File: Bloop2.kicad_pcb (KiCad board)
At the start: 2 copper layers, 15 parts, among them J1 Input, J2 Output, U1 TL072

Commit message: Feature complete device with first layout.
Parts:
- added C5: 1u, Capacitor_THT:CP_Radial_D5.0mm_P2.00mm, F.Cu at (171.4, 118.1)
- added C6: 1u, Capacitor_THT:CP_Radial_D5.0mm_P2.00mm, F.Cu at (135.9, 118.1)
- added D2: D, Diode_THT:D_DO-41_SOD81_P7.62mm_Horizontal, F.Cu at (153.7, 80.0)
- added J3: Input, Connector_Wire:SolderWirePad_1x02_P3.81mm_Drill1mm, F.Cu at (170.2, 82.5)
- added J4: Return, Connector_Wire:SolderWirePad_1x02_P3.81mm_Drill1mm, F.Cu at (137.2, 82.5)
- added J5: Send, Connector_Wire:SolderWirePad_1x02_P3.81mm_Drill1mm, F.Cu at (170.2, 129.5)
- added J6: Output, Connector_Wire:SolderWirePad_1x02_P3.81mm_Drill1mm, F.Cu at (137.2, 129.5)
- added R7: 10k, Resistor_THT:R_Axial_DIN0204_L3.6mm_D1.6mm_P7.62mm_Horizontal, F.Cu at (132.1, 105.4)
- added R8: 47k, Resistor_THT:R_Axial_DIN0204_L3.6mm_D1.6mm_P7.62mm_Horizontal, F.Cu at (175.3, 110.5)
- added R9: 47k, Resistor_THT:R_Axial_DIN0204_L3.6mm_D1.6mm_P7.62mm_Horizontal, F.Cu at (132.1, 110.5)
- added RV2: 10k, Connector_Wire:SolderWirePad_1x03_P3.175mm_Drill1mm, F.Cu at (133.3, 124.5)
- added SW1: 3PDT-A, Connector_Wire:SolderWirePad_1x03_P3.175mm_Drill1mm, F.Cu at (161.3, 120.7)
- added SW2: 3PDT-B, Connector_Wire:SolderWirePad_1x03_P3.175mm_Drill1mm, F.Cu at (174.0, 87.6)
- added SW3: 3PDT-C, Connector_Wire:SolderWirePad_1x03_P3.175mm_Drill1mm, F.Cu at (146.1, 114.3)
- C1: value 1u -> 47u; footprint Capacitor_THT:CP_Radial_D4.0mm_P2.00mm -> Capacitor_THT:CP_Radial_D6.3mm_P2.50mm
- C2: value 100u -> 47u; footprint Capacitor_THT:CP_Radial_D5.0mm_P2.00mm -> Capacitor_THT:CP_Radial_D6.3mm_P2.50mm
- C3: value 47u -> 1u; footprint Capacitor_THT:CP_Radial_D4.0mm_P2.00mm -> Capacitor_THT:CP_Radial_D5.0mm_P2.00mm
- C4: footprint Capacitor_THT:CP_Radial_D4.0mm_P2.00mm -> Capacitor_THT:CP_Radial_D5.0mm_P2.00mm
- D1: value D -> LED; footprint Diode_THT:D_DO-34_SOD68_P7.62mm_Horizontal -> LED_THT:LED_D5.0mm
- J1: value Input -> Power In; footprint Connector_Audio:Jack_3.5mm_CUI_SJ1-3533NG_Horizontal_CircularHoles -> Connector_BarrelJack:BarrelJack_CUI_PJ-102AH_Horizontal
- J2: value Output -> Power Out; footprint Connector_Audio:Jack_3.5mm_CUI_SJ1-3533NG_Horizontal_CircularHoles -> Connector_BarrelJack:BarrelJack_CUI_PJ-102AH_Horizontal
- R1: value 100k -> 2k7
- R4, R5: value 10k -> 100k
- R6: value 22k -> 10k
- RV1: footprint Connector_Wire:SolderWirePad_1x03_P3.175mm_Drill0.8mm -> Connector_Wire:SolderWirePad_1x03_P3.175mm_Drill1mm
- moved J1 67.6 mm to (165.1, 76.2), turned to 180 degrees
- moved C3 59.8 mm to (171.4, 100.3), turned to 90 degrees
- moved C2 49.4 mm to (160.0, 86.4), turned to 90 degrees
- moved J2 44.4 mm to (142.2, 76.2), turned to 180 degrees
- moved R6 41.4 mm to (175.3, 105.4), turned to 180 degrees
- moved R4 40.6 mm to (175.3, 92.7), turned to 180 degrees
- moved D1 34.9 mm to (153.7, 118.1), turned to 90 degrees
- moved C1 30.2 mm to (147.3, 86.4), turned to 90 degrees
- moved RV1 29.5 mm to (174.0, 124.5), turned to 180 degrees
- moved R1 29.0 mm to (149.9, 123.2)
- moved R3 26.2 mm to (156.2, 92.7), turned to 0 degrees
- moved R2 25.3 mm to (143.5, 92.7), turned to 0 degrees
- moved U1 14.4 mm to (157.5, 106.7), turned to 180 degrees
- moved C4 14.2 mm to (135.9, 100.3)
- moved R5 7.62 mm to (132.1, 92.7)
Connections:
- C1 pad 1: Net-(C1-Pad1) -> +9V
- C1 pad 2: Net-(C1-Pad2) -> GND
- C2 pad 1: +9V -> VREF
- C3 pad 2: GND -> Net-(C3-Pad2)
- D1 pad 1: +9V -> Net-(D1-Pad1)
- D1 pad 2: GND -> +9V
- R1 pad 1: Net-(C1-Pad2) -> Net-(D1-Pad1)
- R1 pad 2: GND -> Net-(R1-Pad2)
- R2 pad 2: Net-(C3-Pad1) -> VREF
- R3 pad 1: Net-(C3-Pad1) -> VREF
- R4 pad 1: Net-(C1-Pad1) -> Net-(C3-Pad2)
- R4 pad 2: Net-(C3-Pad1) -> GND
- R5 pad 1: Net-(C3-Pad1) -> Net-(C4-Pad2)
- R5 pad 2: Net-(R5-Pad2) -> GND
- R6 pad 1: Net-(R5-Pad2) -> Net-(C3-Pad1)
- R6 pad 2: Net-(C4-Pad2) -> Net-(R6-Pad2)
- RV1 pad 1: Net-(C4-Pad1) -> Net-(C5-Pad1)
- RV1 pad 2: Net-(J2-PadT) -> Net-(J5-Pad1)
- U1 pad 1: Net-(C4-Pad2) -> Net-(C5-Pad2)
- U1 pad 2: Net-(R5-Pad2) -> Net-(R6-Pad2)
- U1 pad 3: Net-(C1-Pad1) -> VREF
- U1 pad 5: (no net) -> VREF
- U1 pad 6: (no net) -> Net-(R7-Pad2)
- U1 pad 7: (no net) -> Net-(C6-Pad2)
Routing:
- net GNDPWR: track 0.00 -> 142.2 mm
- net +9V: track 0.00 -> 76.2 mm
- net VREF: track 0.00 -> 33.2 mm
- net Net-(R7-Pad2): track 0.00 -> 21.5 mm
- net Net-(R6-Pad2): track 0.00 -> 20.4 mm
- net Net-(C6-Pad2): track 0.00 -> 20.0 mm
- net Net-(C5-Pad2): track 0.00 -> 19.6 mm
- net Net-(C4-Pad2): track 0.00 -> 19.5 mm
- net Net-(J6-Pad1): track 0.00 -> 16.6 mm
- net Net-(RV2-Pad2): track 0.00 -> 14.1 mm
- net Net-(C3-Pad2): track 0.00 -> 12.8 mm
- net Net-(R1-Pad2): track 0.00 -> 7.93 mm
- net Net-(C5-Pad1): track 0.00 -> 7.40 mm
- net Net-(C6-Pad1): track 0.00 -> 7.40 mm
- net Net-(D1-Pad1): track 0.00 -> 7.33 mm
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- added copper zone on B.Cu, net GND
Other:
- board outline added: 50.8 x 68.6 mm
- rule pad_to_mask_clearance: 0.051 -> 0

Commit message: Improved, compacted layout.
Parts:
- D2: value D -> 40V
- J1, J2: footprint Connector_BarrelJack:BarrelJack_CUI_PJ-102AH_Horizontal -> Connector_Wire:SolderWirePad_1x02_P3.81mm_Drill0.8mm
- J3, J4, J5, J6: footprint Connector_Wire:SolderWirePad_1x02_P3.81mm_Drill1mm -> Connector_Wire:SolderWirePad_1x01_Drill0.8mm
- R8, R9: value 47k -> 100k
- RV1, RV2: footprint Connector_Wire:SolderWirePad_1x03_P3.175mm_Drill1mm -> Potentiometer_THT:Potentiometer_Bourns_PTV09A-1_Single_Vertical
- SW1: value 3PDT-A -> 3PDTA; footprint Connector_Wire:SolderWirePad_1x03_P3.175mm_Drill1mm -> Connector_Wire:SolderWirePad_1x02_P3.81mm_Drill1mm
- SW2: value 3PDT-B -> 3PDTB; footprint Connector_Wire:SolderWirePad_1x03_P3.175mm_Drill1mm -> Connector_Wire:SolderWirePad_1x02_P3.81mm_Drill1mm
- SW3: value 3PDT-C -> 3PDTC; footprint Connector_Wire:SolderWirePad_1x03_P3.175mm_Drill1mm -> Connector_Wire:SolderWirePad_1x02_P3.81mm_Drill1mm
- moved RV2 62.5 mm to (175.3, 78.1), turned to 90 degrees
- moved J6 62.2 mm to (177.2, 81.9), turned to 0 degrees
- moved J5 54.9 mm to (142.9, 81.9)
- moved RV1 52.3 mm to (149.9, 78.1), turned to 90 degrees
- moved C6 50.7 mm to (175.9, 87.0), turned to 270 degrees
- moved R9 48.2 mm to (177.2, 93.3), turned to 180 degrees
- moved J4 47.4 mm to (177.2, 108.0), turned to 0 degrees
- moved R7 45.8 mm to (177.2, 97.2), turned to 180 degrees
- moved SW3 42.4 mm to (173.4, 81.9), turned to 180 degrees
- moved SW1 41.4 mm to (146.7, 81.9), turned to 0 degrees
- moved C5 41.4 mm to (144.1, 87.0), turned to 270 degrees
- moved R1 40.6 mm to (163.8, 85.1), turned to 180 degrees
- moved C4 38.8 mm to (174.6, 101.6), turned to 270 degrees
- moved R5 37.6 mm to (168.9, 100.3), turned to 270 degrees
- moved D1 37.4 mm to (160.0, 81.3)
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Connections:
- SW3 pad 1: Net-(RV2-Pad2) -> Net-(J6-Pad1)
- SW3 pad 2: Net-(J6-Pad1) -> Net-(RV2-Pad2)
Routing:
- net GNDPWR: track 142.2 -> 0.00 mm
- net +9V: track 76.2 -> 47.8 mm
- net Net-(J6-Pad1): track 16.6 -> 3.81 mm
- net Net-(RV2-Pad2): track 14.1 -> 4.88 mm
- net Net-(C4-Pad2): track 19.5 -> 12.5 mm
- net Net-(C5-Pad1): track 7.40 -> 12.8 mm
- net Net-(C3-Pad2): track 12.8 -> 17.1 mm
- net Net-(C6-Pad1): track 7.40 -> 11.5 mm
- net Net-(J5-Pad1): track 5.34 -> 9.42 mm
- net Net-(R6-Pad2): track 20.4 -> 18.6 mm
- net Net-(C6-Pad2): track 20.0 -> 21.3 mm
- net Net-(C4-Pad1): track 6.66 -> 5.53 mm
- net Net-(D1-Pad1): track 7.33 -> 6.21 mm
- net VREF: track 33.2 -> 32.7 mm
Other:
- board size 50.8 x 68.6 mm -> 40.6 x 49.5 mm
- net class Default: trace_width 0.25 -> 0.5
- board text added: "Dual Boost Loop Switcher"
- board text added: "rlk 2019"

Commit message: Tuned layout.
The moment you send a PCB off for printing, you think of a ton of obvious ideas for improvement.
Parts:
- removed J2: Power Out, Connector_Wire:SolderWirePad_1x02_P3.81mm_Drill0.8mm
- J1: footprint Connector_Wire:SolderWirePad_1x02_P3.81mm_Drill0.8mm -> Connector_Wire:SolderWirePad_1x02_P3.81mm_Drill1mm
- J3, J4, J5, J6: footprint Connector_Wire:SolderWirePad_1x01_Drill0.8mm -> Connector_Wire:SolderWirePad_1x01_Drill1mm
- moved J3 19.1 mm to (161.9, 107.3)
- moved J5 15.2 mm to (142.9, 66.7)
- moved J6 15.2 mm to (177.2, 66.7)
- moved SW1 15.2 mm to (146.7, 66.7)
- moved SW3 15.2 mm to (173.4, 66.7)
- moved R1 14.4 mm to (154.3, 74.3), turned to 90 degrees
- moved J4 11.4 mm to (165.7, 107.3)
- moved R2 10.9 mm to (163.8, 79.4)
- moved D2 9.16 mm to (165.1, 66.7), turned to 270 degrees
- moved D1 8.35 mm to (158.8, 73.0), turned to 0 degrees
- moved U1 6.98 mm to (156.2, 94.6)
- moved J1 6.35 mm to (161.3, 66.7), turned to 180 degrees
- moved SW2 6.29 mm to (154.3, 107.3), turned to 0 degrees
- moved RV1 5.71 mm to (149.9, 83.8)
- moved RV2 5.71 mm to (175.3, 83.8)
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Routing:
- net +9V: track 47.8 -> 33.8 mm
- net Net-(RV2-Pad2): track 4.88 -> 18.5 mm
- net Net-(C6-Pad2): track 21.3 -> 11.4 mm
- net Net-(J5-Pad1): track 9.42 -> 19.0 mm
- net Net-(C5-Pad2): track 19.4 -> 10.3 mm
- net Net-(C5-Pad1): track 12.8 -> 5.36 mm
- net Net-(R7-Pad2): track 21.1 -> 13.8 mm
- net Net-(C6-Pad1): track 11.5 -> 5.89 mm
- net Net-(R6-Pad2): track 18.6 -> 13.3 mm
- net Net-(C3-Pad2): track 17.1 -> 12.5 mm
- net Net-(C4-Pad1): track 5.53 -> 9.83 mm
- net Net-(R1-Pad2): track 7.67 -> 3.81 mm
- net Net-(C3-Pad1): track 6.26 -> 9.83 mm
- net VREF: track 32.7 -> 31.1 mm
- net Net-(J3-Pad1): track 5.39 -> 3.81 mm
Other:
- board size 40.6 x 49.5 mm -> 40.6 x 45.7 mm
- board text added: "In"
- board text added: "Out"
- board text added: "Ret"
- board text added: "Send"

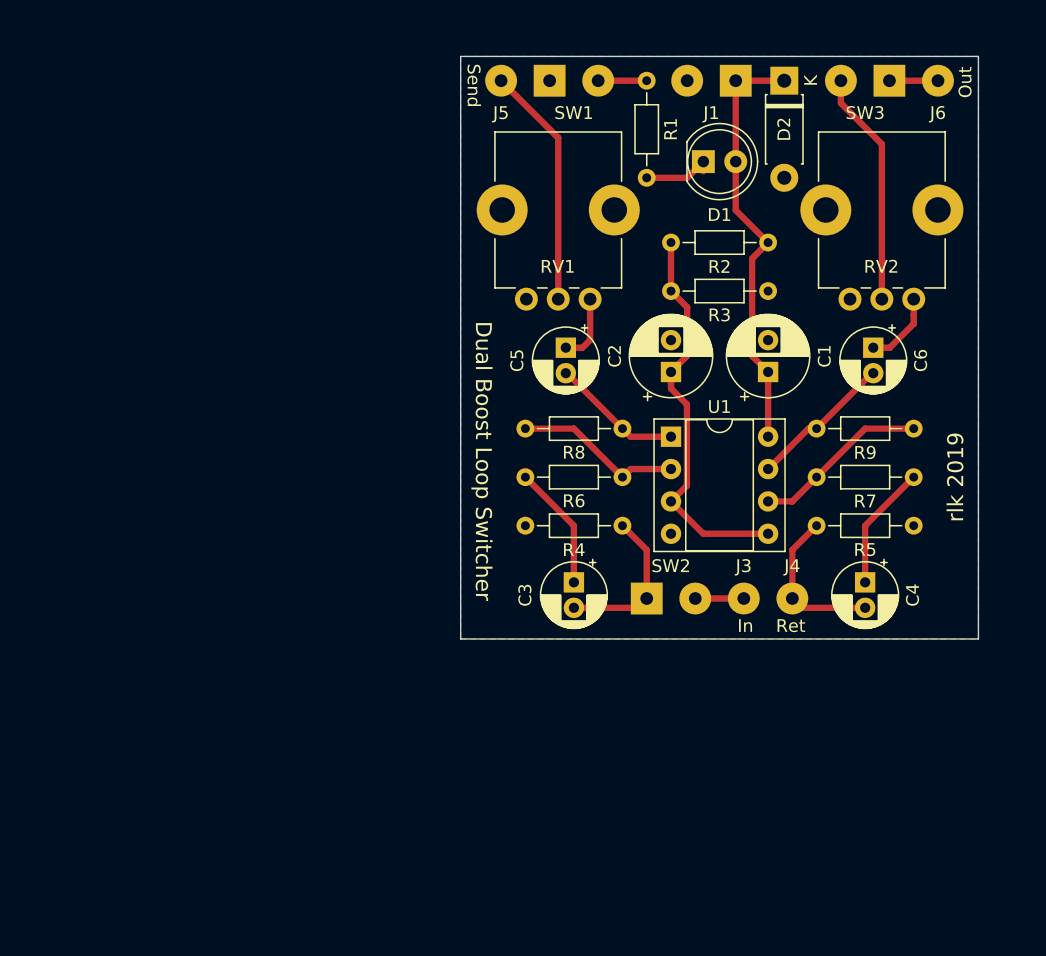
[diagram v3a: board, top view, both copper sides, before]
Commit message: Fix design flaws detected in previous circuit.
A previous design was printed and fabricated, revealing a number of problems.

1. The pots were not appropriate for panel mounting. They were too short, leaving no room for the electrolitic capacitors.
2. The switches were backwards on the schematic (easily resolvable in the wiring).
3. The circuit cut the highs too much. This revision matches the input RC to the Timmy.

This design mounts the footswitch on the PCB, which should give a secure enclosure mounting.
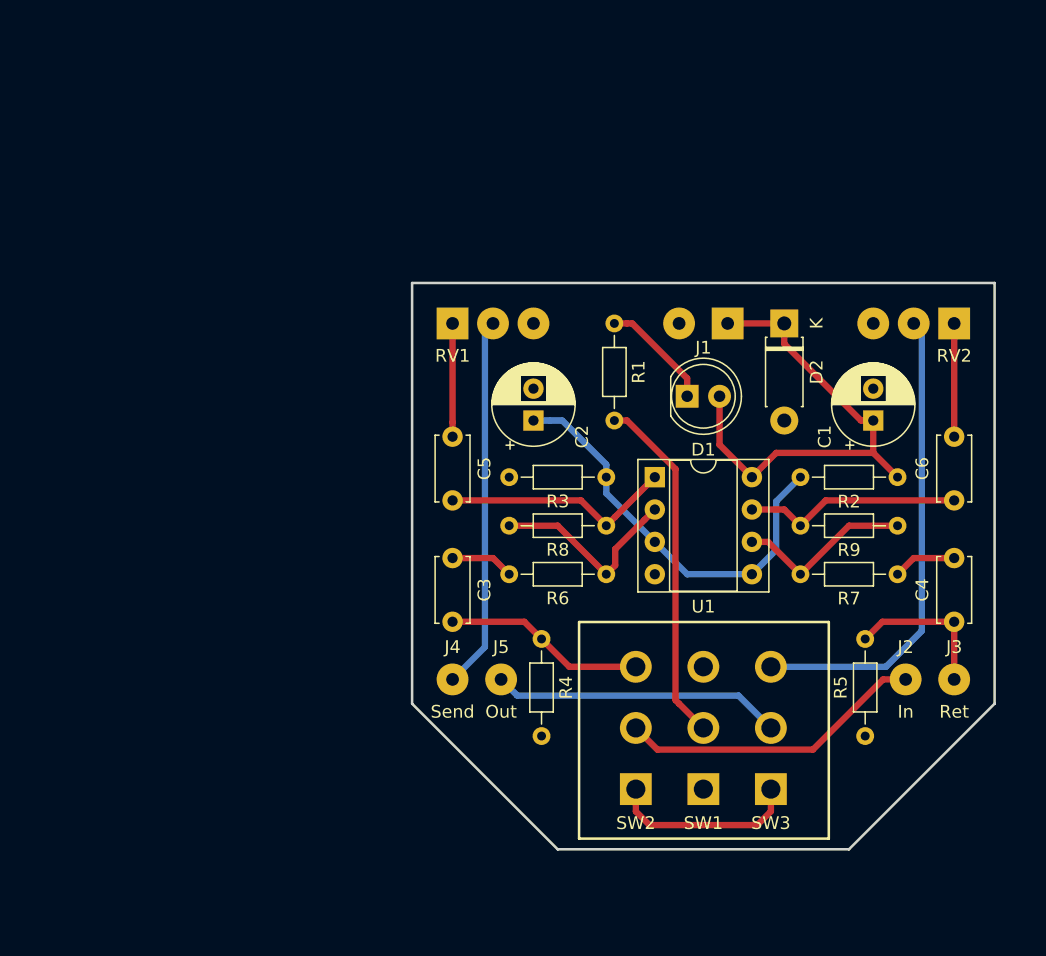
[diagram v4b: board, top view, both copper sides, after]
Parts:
- removed J6: Output, Connector_Wire:SolderWirePad_1x01_Drill1mm
- added J2: Input, Connector_Wire:SolderWirePad_1x01_Drill1mm, F.Cu at (174.6, 113.7)
- C3, C4: value 1u -> 47n; footprint Capacitor_THT:CP_Radial_D5.0mm_P2.00mm -> Capacitor_THT:C_Disc_D5.0mm_W2.5mm_P5.00mm
- C5, C6: footprint Capacitor_THT:CP_Radial_D5.0mm_P2.00mm -> Capacitor_THT:C_Disc_D5.0mm_W2.5mm_P5.00mm
- J3: value Input -> Return
- J4: value Return -> Send
- J5: value Send -> Output
- R4, R5: value 100k -> 2M2
- RV1, RV2: footprint Potentiometer_THT:Potentiometer_Bourns_PTV09A-1_Single_Vertical -> Connector_Wire:SolderWirePad_1x03_P3.175mm_Drill1mm
- SW1, SW2, SW3: footprint Connector_Wire:SolderWirePad_1x02_P3.81mm_Drill1mm -> Custom:SolderWirePad_1x03_P9.60mm_Drill1.5mm
- moved SW1 56.9 mm to (158.8, 122.3)
- moved SW3 56.4 mm to (164.1, 122.3), turned to 0 degrees
- moved J5 47.0 mm to (142.9, 113.7)
- moved J4 27.4 mm to (139.1, 113.7)
- moved R2 21.0 mm to (174.0, 97.8)
- moved J1 19.1 mm to (160.7, 85.7)
- moved D2 19.0 mm to (165.1, 85.7)
- moved D1 18.5 mm to (157.5, 91.4)
- moved J3 17.7 mm to (178.4, 113.7)
- moved R3 15.5 mm to (151.1, 97.8), turned to 180 degrees
- moved SW2 15.0 mm to (153.4, 122.3)
- moved R1 11.7 mm to (151.8, 85.7), turned to 270 degrees
- moved C2 11.4 mm to (145.4, 93.3)
- moved C5 11.3 mm to (139.1, 94.6)
- moved RV1 11.0 mm to (139.1, 85.7), turned to 0 degrees
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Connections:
- J3 pad 1: Net-(J3-Pad1) -> Net-(C4-Pad2)
- J4 pad 1: Net-(C4-Pad2) -> Net-(J4-Pad1)
- RV1 pad 2: Net-(J5-Pad1) -> Net-(J4-Pad1)
- SW1 pad 1: GND -> (no net)
- SW2 pad 1: Net-(C3-Pad2) -> BYPASS
- SW2 pad 2: Net-(J3-Pad1) -> Net-(J2-Pad1)
- SW3 pad 1: Net-(J6-Pad1) -> BYPASS
- SW3 pad 2: Net-(RV2-Pad2) -> Net-(J5-Pad1)
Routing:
- net Net-(J4-Pad1): track 0.00 -> 29.3 mm
- net Net-(J2-Pad1): track 0.00 -> 24.2 mm
- net Net-(R1-Pad2): track 3.81 -> 27.6 mm
- net Net-(RV2-Pad2): track 18.5 -> 37.4 mm
- net BYPASS: track 0.00 -> 15.0 mm
- net Net-(C5-Pad2): track 10.3 -> 18.3 mm
- net Net-(C6-Pad2): track 11.4 -> 17.2 mm
- net Net-(C4-Pad1): track 9.83 -> 4.97 mm
- net Net-(C3-Pad1): track 9.83 -> 4.97 mm
- net +9V: track 33.8 -> 38.5 mm
- net Net-(J6-Pad1): track 3.81 -> 0.00 mm
- net Net-(J3-Pad1): track 3.81 -> 0.00 mm
- net Net-(J5-Pad1): track 19.0 -> 22.8 mm
- net Net-(C5-Pad1): track 5.36 -> 8.89 mm
- net Net-(C3-Pad2): track 12.5 -> 15.8 mm
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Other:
- board size 40.6 x 45.7 mm -> 45.7 x 44.5 mm
- board text added: "Boosted Loop Switcher rlk 2019"
- board text removed: "Dual Boost Loop Switcher"
- board text removed: "rlk 2019"

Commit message: PCB layout draft
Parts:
- added C7: 10u, Capacitor_THT:CP_Radial_D4.0mm_P2.00mm, F.Cu at (139.1, 92.7)
- added C8: 10u, Capacitor_THT:CP_Radial_D4.0mm_P2.00mm, F.Cu at (177.2, 92.1)
- added R10: 22k, Resistor_THT:R_Axial_DIN0204_L3.6mm_D1.6mm_P7.62mm_Horizontal, F.Cu at (167.0, 105.4)
- added RLED1: 360, Resistor_THT:R_Axial_DIN0204_L3.6mm_D1.6mm_P7.62mm_Horizontal, F.Cu at (153.0, 92.7)
- C3, C4: value 47n -> 1u
- C5, C6: value 1u -> 47u; footprint Capacitor_THT:C_Disc_D5.0mm_W2.5mm_P5.00mm -> Capacitor_THT:CP_Radial_D6.3mm_P2.50mm
- R1: value 2k7 -> 10k
- R3, R6: value 10k -> 100k
- R4, R5: value 2M2 -> 100k
- R7: value 10k -> 2k2
- R8: value 100k -> 2k2
- R9: value 100k -> 22k
- moved J2 46.5 mm to (136.5, 87.0)
- moved J5 43.4 mm to (177.2, 87.0)
- moved C2 40.0 mm to (179.1, 114.9), turned to 270 degrees
- moved C1 39.5 mm to (139.1, 114.9), turned to 270 degrees
- moved R6 31.1 mm to (174.6, 105.4), turned to 90 degrees
- moved R5 29.0 mm to (142.9, 105.4), turned to 90 degrees
- moved R8 27.6 mm to (170.8, 105.4), turned to 90 degrees
- moved R7 27.3 mm to (146.7, 105.4), turned to 90 degrees
- moved C5 27.1 mm to (144.1, 121.3)
- moved C6 27.1 mm to (173.4, 121.3)
- moved J3 26.8 mm to (181.0, 87.0)
- moved J4 26.7 mm to (140.3, 87.0)
- moved R4 25.4 mm to (171.4, 109.9)
- moved R9 23.8 mm to (150.5, 105.4), turned to 90 degrees
- moved R1 23.4 mm to (139.1, 105.4), turned to 90 degrees
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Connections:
- C5 pad 2: Net-(C5-Pad2) -> GND
- C6 pad 2: Net-(C6-Pad2) -> GND
- R1 pad 1: Net-(D1-Pad1) -> +9V
- R1 pad 2: Net-(R1-Pad2) -> VREF
- R2 pad 1: +9V -> VREF
- R2 pad 2: VREF -> GND
- R3 pad 1: VREF -> Net-(C3-Pad2)
- R4 pad 1: Net-(C3-Pad2) -> Net-(C4-Pad2)
- R5 pad 1: Net-(C4-Pad2) -> Net-(C3-Pad1)
- R5 pad 2: GND -> VREF
- R6 pad 1: Net-(C3-Pad1) -> Net-(C4-Pad1)
- R6 pad 2: Net-(R6-Pad2) -> VREF
- R7 pad 1: Net-(C4-Pad1) -> Net-(R7-Pad1)
- R7 pad 2: Net-(R7-Pad2) -> Net-(C5-Pad1)
- R8 pad 1: Net-(R6-Pad2) -> Net-(R10-Pad1)
- R8 pad 2: Net-(C5-Pad2) -> Net-(C6-Pad1)
- R9 pad 1: Net-(R7-Pad2) -> Net-(R7-Pad1)
- R9 pad 2: Net-(C6-Pad2) -> Net-(C7-Pad2)
- RV1 pad 1: Net-(C5-Pad1) -> Net-(C7-Pad1)
- RV2 pad 1: Net-(C6-Pad1) -> Net-(C8-Pad1)
- SW1 pad 2: Net-(R1-Pad2) -> Net-(RLED1-Pad2)
- U1 pad 1: Net-(C5-Pad2) -> Net-(C7-Pad2)
- U1 pad 2: Net-(R6-Pad2) -> Net-(R7-Pad1)
- U1 pad 3: VREF -> Net-(C3-Pad1)
- U1 pad 5: VREF -> Net-(C4-Pad1)
- U1 pad 6: Net-(R7-Pad2) -> Net-(R10-Pad1)
- U1 pad 7: Net-(C6-Pad2) -> Net-(C8-Pad2)
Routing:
- net Net-(RLED1-Pad2): track 0.00 -> 34.3 mm
- net Net-(R1-Pad2): track 27.6 -> 0.00 mm
- net VREF: track 32.7 -> 58.3 mm
- net Net-(J2-Pad1): track 24.2 -> 43.0 mm
- net Net-(J4-Pad1): track 29.3 -> 10.9 mm
- net Net-(C5-Pad2): track 18.3 -> 0.00 mm
- net Net-(C7-Pad2): track 0.00 -> 17.7 mm
- net Net-(C4-Pad2): track 12.1 -> 29.5 mm
- net Net-(C3-Pad1): track 4.97 -> 22.3 mm
- net Net-(C6-Pad2): track 17.2 -> 0.00 mm
- net Net-(C8-Pad2): track 0.00 -> 17.2 mm
- net +9V: track 38.5 -> 54.8 mm
- net Net-(C4-Pad1): track 4.97 -> 21.2 mm
- net Net-(C5-Pad1): track 8.89 -> 25.1 mm
- net Net-(R6-Pad2): track 15.9 -> 0.00 mm
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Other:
- board size 45.7 x 44.5 mm -> 49.5 x 43.8 mm
- board text added: "Out Vol"
- board text added: "Power"
- board text added: "Send Vol"
- board text removed: "Boosted Loop Switcher rlk 2019"
